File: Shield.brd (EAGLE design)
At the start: 99.1 x 53.3 mm, 71 parts

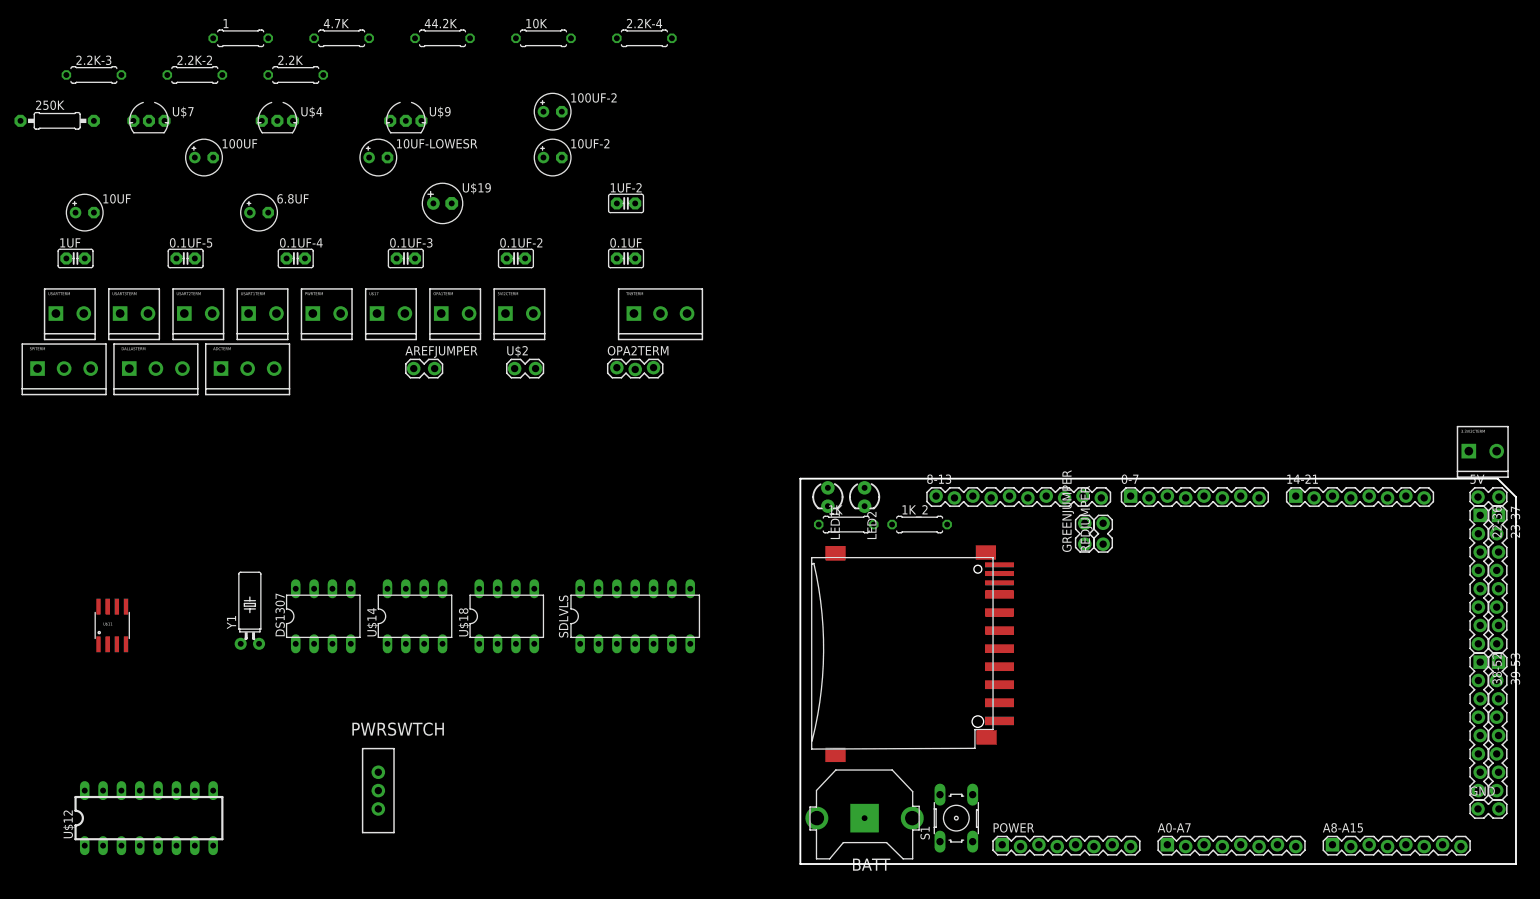
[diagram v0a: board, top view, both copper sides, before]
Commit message: All components on board
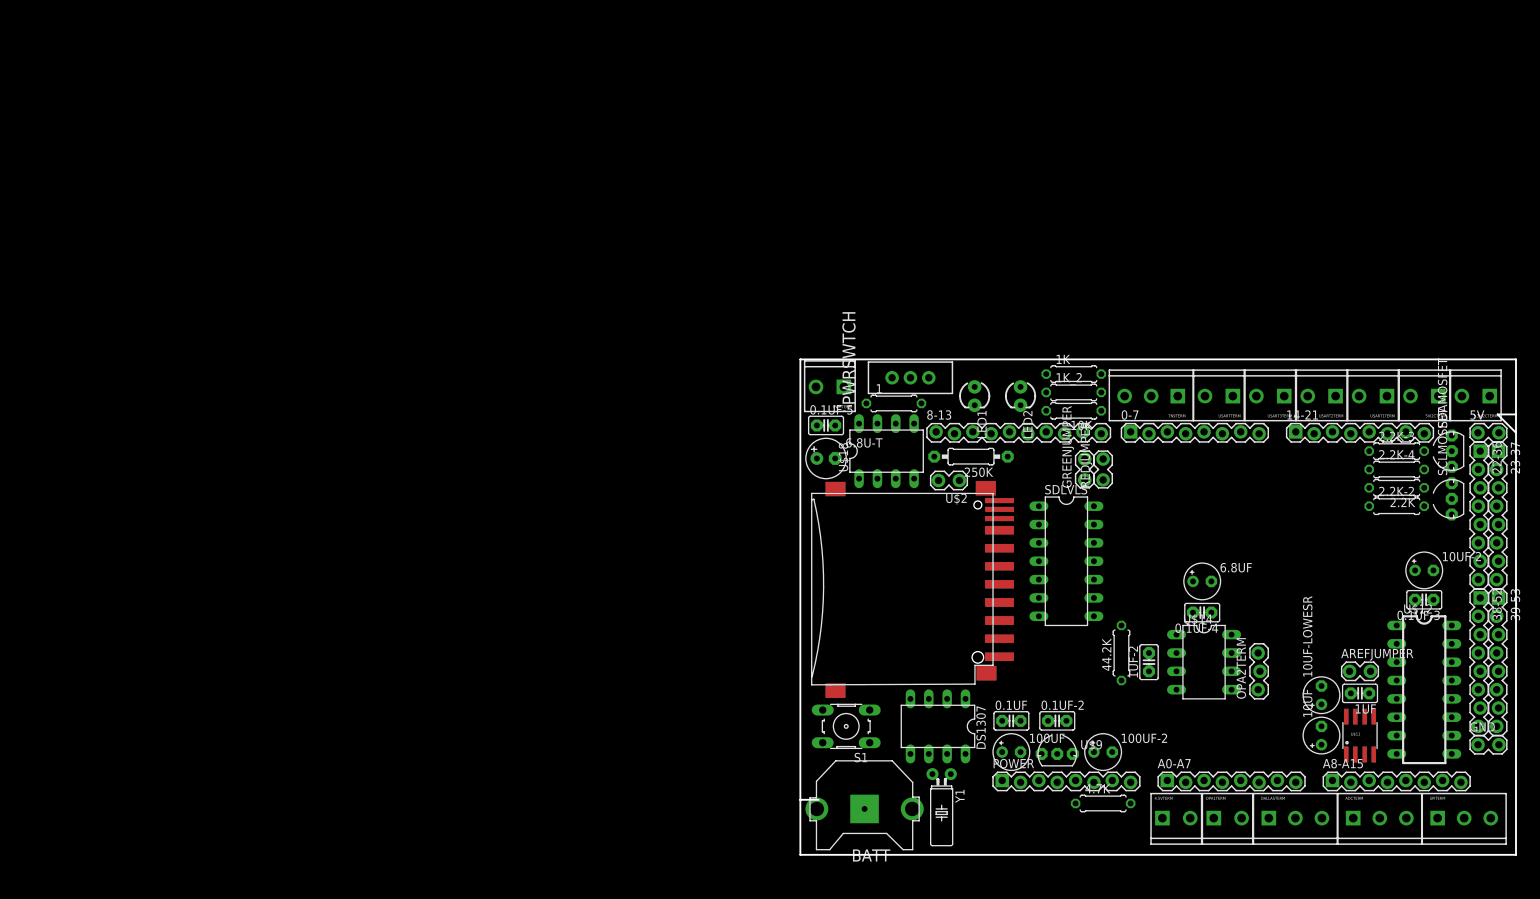
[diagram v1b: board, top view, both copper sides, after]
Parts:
- removed U$17: 2PINHEADERS, LEMS:SCREWTERMINAL-3.5MM-2_LOCK
- removed U$19: ELECTROLYTICCAPL, LEMS:E2,5-6
- removed U$4, U$7: MOSFETNN, LEMS:TO-92INLINE
- added 4.5VTERM: 2PINHEADERS, LEMS:SCREWTERMINAL-3.5MM-2_LOCK
- added 6.8U-T: ELECTROLYTICCAPL, LEMS:E2,5-6
- added SCLMOSFET, SDAMOSFET: MOSFETNN, LEMS:TO-92INLINE
- moved SPITERM 203.5 mm to (88.4, 6.35)
- moved 1UF 187.7 mm to (77.5, 23.6), turned to 180 degrees
- moved 2.2K-3 187.7 mm to (82.5, 57.1)
- moved 10UF 185.9 mm to (72.1, 17.8), turned to 90 degrees
- moved U$12 177.4 mm to (86.4, 24.1), turned to 270 degrees
- moved 2.2K-2 176.8 mm to (82.5, 49.5)
- moved U$11 173.4 mm to (77.5, 17.8)
- moved DALLASTERM 169.6 mm to (65.0, 6.35)
- moved ADCTERM 168.6 mm to (76.7, 6.35)
- moved USARTTERM 163.0 mm to (59.7, 64.8), turned to 180 degrees
- moved 2.2K 162.8 mm to (82.5, 52.1), turned to 180 degrees
- moved USART3TERM 161.2 mm to (66.8, 64.8), turned to 180 degrees
- moved USART2TERM 159.4 mm to (73.9, 64.8), turned to 180 degrees
- moved USART1TERM 157.6 mm to (81.0, 64.8), turned to 180 degrees
- moved 10UF-LOWESR 150.3 mm to (72.1, 23.4), turned to 90 degrees
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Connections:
- net 3.3V: now also SCLMOSFET.2, SDAMOSFET.2; no longer U$4.2, U$7.2
- net 3.3V_SCL: now also SCLMOSFET.1; no longer U$7.1
- net 3.3V_SDA: now also SDAMOSFET.1; no longer U$4.1
- net 4.5V: now also 4.5VTERM.1, 4.5VTERM.2; no longer U$17.1, U$17.2
- net 5V: now also 6.8U-T.+; no longer U$19.+
- net N$7: now also 6.8U-T.-; no longer U$19.-
- net RX0: now also USARTTERM.1; no longer USARTTERM.2
- net RX1: now also USART1TERM.1; no longer USART1TERM.2
- net RX2: now also USART2TERM.1; no longer USART2TERM.2
- net RX3: now also USART3TERM.1; no longer USART3TERM.2
- net SCL: now also SCLMOSFET.3; no longer U$7.3
- net SDA: now also SDAMOSFET.3; no longer U$4.3
- net TN9_ACT: now also TN9TERM.3; no longer TN9TERM.1
- net TN9_DATA: now also TN9TERM.1; no longer TN9TERM.3
- net TX0: now also USARTTERM.2; no longer USARTTERM.1
- net TX1: now also USART1TERM.2; no longer USART1TERM.1
- net TX2: now also USART2TERM.2; no longer USART2TERM.1
- net TX3: now also USART3TERM.2; no longer USART3TERM.1
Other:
- board size 99.1 x 53.3 mm -> 99.1 x 68.6 mm

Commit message: Started Routing
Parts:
- 0-7, 14-21, 22-36, 23-37, 38-52, 39-53, A0-A7, A8-A15, POWER: value 8PINHEADERN -> 8PHN; device LEMS:8PINHEADER -> LEMS:8PH
- 0.1UF, 0.1UF-2, 0.1UF-3, 0.1UF-4, 0.1UF-5, 1UF, 1UF-2: value CERAMICCAPL -> CCL
- 1, 10K, 1K, 1K_2, 2.2K, 2.2K-2, 2.2K-3, 2.2K-4: value RESISTORT -> RT
- 100UF-2, 10UF, 10UF-2, 10UF-LOWESR, 6.8UF: value ELECTROLYTICCAPS -> CES
- 250K: value RESISTORN -> RN
- 3.3VI2CTERM, 4.5VTERM, 5VI2CTERM, OPA1TERM, PWRTERM, USART1TERM, USART2TERM, USART3TERM, USARTTERM: value 2PINHEADERS -> 2PHS
- 5V, GND, U$2: value 2PINHEADERN -> 2PHN; device LEMS:2PINHEADER -> LEMS:2PH
- 6.8U-T: value ELECTROLYTICCAPL -> CES; device LEMS:E2,5-6 -> LEMS:E2,5-5
- 8-13: value 10PINHEADERN -> 10PHN; device LEMS:10PINHEADER -> LEMS:10PH
- ADCTERM, DALLASTERM, SPITERM, TN9TERM: value 3PINHEADERS -> 3PHS
- AREFJUMPER, GREENJUMPER, REDJUMPER: value JUMPER2PINN -> 2PJN; device LEMS:2PINHEADER -> LEMS:2PH
- OPA2TERM: value 3PINHEADERN -> 3PHN; device LEMS:3PINHEADER -> LEMS:3PH
- moved BATT 67.3 mm to (63.5, 47.0), turned to 90 degrees
- moved DS1307 65.4 mm to (76.2, 50.8), turned to 0 degrees
- moved Y1 59.5 mm to (71.6, 41.1), flipped to the bottom, turned to 90 degrees
- moved PWRTERM 57.7 mm to (5.08, 8.38), turned to 270 degrees
- moved S1 54.0 mm to (53.3, 45.7)
- moved 6.8U-T 50.1 mm to (34.5, 16.8), turned to 270 degrees
- moved PWRSWTCH 49.8 mm to (9.65, 17.8), turned to 180 degrees
- moved U$18 47.9 mm to (18.3, 9.65), turned to 270 degrees
- moved 0.1UF-5 47.8 mm to (4.32, 13.0), turned to 180 degrees
- moved 1 47.2 mm to (32.0, 20.6)
- moved 250K 39.7 mm to (18.5, 17.0), flipped to the bottom
- moved 4.7K 31.5 mm to (62.2, 32.5), flipped to the bottom
- moved 0.1UF-3 28.7 mm to (66.0, 16.3)
- moved 10UF-2 27.9 mm to (66.0, 21.6)
- moved 100UF 26.9 mm to (55.9, 19.3)
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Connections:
- removed net N$87: BATT.+1, BATT.+2, DS1307.3
- new net VBAT: BATT.+1, DS1307.3
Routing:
- net GND: track 0.00 -> 79.8 mm
- net SCL: track 0.00 -> 36.9 mm
- net N$8: track 0.00 -> 29.4 mm
- net 3.3V_SCL: track 0.00 -> 28.4 mm
- net 5V: track 0.00 -> 24.7 mm
- net SDA: track 0.00 -> 24.3 mm
- net VBAT: track 0.00 -> 22.3 mm
- net 3.3V_SDA: track 0.00 -> 21.2 mm
- net 3.3V: track 0.00 -> 12.5 mm
- net PWRN: track 0.00 -> 12.4 mm
- net TN9_ACT: track 0.00 -> 10.9 mm
- net TN9_CLK: track 0.00 -> 9.54 mm
- net N$6: track 0.00 -> 8.52 mm
- net N$86: track 0.00 -> 8.34 mm
- net TN9_DATA: track 0.00 -> 8.33 mm
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
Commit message: Improved Routing
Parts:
- moved S1 36.1 mm to (28.4, 19.6), turned to 270 degrees
- moved 1UF 24.2 mm to (53.3, 22.1), turned to 0 degrees
- moved U$11 24.1 mm to (53.3, 17.8), turned to 270 degrees
- moved 0.1UF-2 23.0 mm to (34.0, 21.6), turned to 90 degrees
- moved 0.1UF-3 21.1 mm to (77.5, 34.0)
- moved 100UF-2 19.8 mm to (38.9, 21.6), turned to 90 degrees
- moved 100UF 17.3 mm to (38.9, 16.3), turned to 90 degrees
- moved 44.2K 17.3 mm to (48.5, 32.5)
- moved 4.7K 17.0 mm to (64.8, 15.7), turned to 180 degrees
- moved 1UF-2 16.9 mm to (51.8, 31.2)
- moved 1 14.9 mm to (34.5, 5.84), flipped to the bottom
- moved U$14 13.5 mm to (51.6, 36.8)
- moved 0.1UF-4 13.3 mm to (56.9, 38.9)
- moved 6.8UF 12.8 mm to (61.2, 36.3)
- moved 6.8U-T 12.5 mm to (26.7, 7.11)
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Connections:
- net CH1: now also ADCTERM.1; no longer ADCTERM.3
- net CH3: now also ADCTERM.3; no longer ADCTERM.1
- net MISO: now also SPITERM.1; no longer SPITERM.3
- net MOSI: now also SPITERM.3; no longer SPITERM.2
- net SCK: now also SPITERM.2; no longer SPITERM.1
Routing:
- net GND: track 79.8 -> 286.5 mm
- net 5V: track 24.7 -> 164.9 mm, vias 0 -> 1
- net MOSI: track 0.00 -> 52.2 mm, vias 0 -> 1
- net SCK: track 0.00 -> 44.3 mm, vias 0 -> 1
- net SS: track 0.00 -> 39.7 mm
- net MISO: track 0.00 -> 36.5 mm
- net 4.5V: track 0.00 -> 36.2 mm
- net CH3: track 0.00 -> 28.0 mm
- net CH2: track 0.00 -> 23.8 mm
- net CH1: track 0.00 -> 18.5 mm
- net MISO_SOFT: track 0.00 -> 16.2 mm
- net 3.3V: track 12.5 -> 27.1 mm
- net RESET: track 0.00 -> 12.2 mm
- net N$83: track 0.00 -> 11.0 mm
- net REDLED2: track 0.00 -> 6.73 mm
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
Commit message: Continued routing
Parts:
- moved 0.1UF-3 14.5 mm to (66.0, 25.1), flipped to the bottom
- moved 1UF-2 12.9 mm to (39.1, 29.2), flipped to the bottom, turned to 180 degrees
- moved 10UF 12.8 mm to (48.0, 22.9), turned to 270 degrees
- moved U$2 10.0 mm to (22.6, 56.4)
- moved 10UF-LOWESR 9.52 mm to (60.5, 20.3), turned to 270 degrees
- moved 44.2K 9.40 mm to (39.1, 32.8), turned to 0 degrees
- moved 10UF-2 9.30 mm to (66.3, 20.3), turned to 270 degrees
- moved 0.1UF-4 7.95 mm to (64.0, 35.3), turned to 0 degrees
- moved 6.8UF 5.68 mm to (63.8, 31.2)
- moved AREFJUMPER 5.68 mm to (74.9, 34.3)
- moved U$14 5.24 mm to (50.3, 31.8)
- moved OPA2TERM 2.84 mm to (58.4, 27.9)
- moved 1UF 0.76 mm to (53.3, 22.9), turned to 270 degrees
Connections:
- net 5V: now also 10UF-2.+; no longer 10UF-2.-
- net GND: now also 10UF-2.-; no longer 10UF-2.+
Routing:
- net GND: track 286.5 -> 380.7 mm, vias 0 -> 1
- net 3.3V: track 27.1 -> 102.2 mm, vias 0 -> 2
- net SS_SOFT: track 0.00 -> 20.6 mm
- net SD_CSIN: track 0.00 -> 20.4 mm
- net MOSI_SOFT: track 0.00 -> 20.2 mm
- net 5V: track 164.9 -> 185.1 mm
- net SCK_SOFT: track 0.00 -> 14.9 mm, vias 0 -> 1
- net SD_CD: track 0.00 -> 14.6 mm
- net SD_SCKIN: track 0.00 -> 13.1 mm
- net SD_DATAIN: track 0.00 -> 12.2 mm
- net SD_WP: track 0.37 -> 11.2 mm
- net N$1: track 0.00 -> 8.49 mm
- net 4.5V: track 36.2 -> 41.9 mm
- net MISO_SOFT: track 16.2 -> 17.0 mm

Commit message: Almost complete routing
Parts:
- moved OPA1TERM 74.9 mm to (5.08, 59.9), turned to 270 degrees
- moved 0.1UF-4 15.0 mm to (50.3, 41.4), turned to 180 degrees
- moved 10K 11.3 mm to (50.3, 38.6), flipped to the bottom, turned to 0 degrees
- moved 6.8UF 8.27 mm to (58.2, 37.3), turned to 90 degrees
- moved 4.5VTERM 7.11 mm to (57.4, 6.35)
- moved 1UF-2 3.82 mm to (38.9, 33.0), flipped to the top
- moved 44.2K 2.81 mm to (38.9, 30.0), flipped to the bottom
- moved OPA2TERM 1.02 mm to (57.4, 27.9)
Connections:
- net GND: now also OPA1TERM.2; no longer OPA1TERM.1
- net LIOP-: now also OPA1TERM.1; no longer OPA1TERM.2
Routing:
- net GND: track 380.7 -> 481.4 mm
- net LIOP-: track 0.00 -> 68.1 mm
- net 5V: track 185.1 -> 252.7 mm
- net CH0: track 0.00 -> 58.8 mm
- net 3.3V: track 102.2 -> 151.2 mm
- net D39: track 0.00 -> 36.4 mm, vias 0 -> 1
- net 4.5V: track 41.9 -> 75.2 mm
- net SS_SOFT: track 20.6 -> 26.5 mm
- net N$3: track 0.00 -> 3.43 mm
- net N$4: track 0.00 -> 3.18 mm
- net N$2: track 0.00 -> 3.18 mm
